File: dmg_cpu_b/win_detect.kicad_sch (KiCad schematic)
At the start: 127 parts

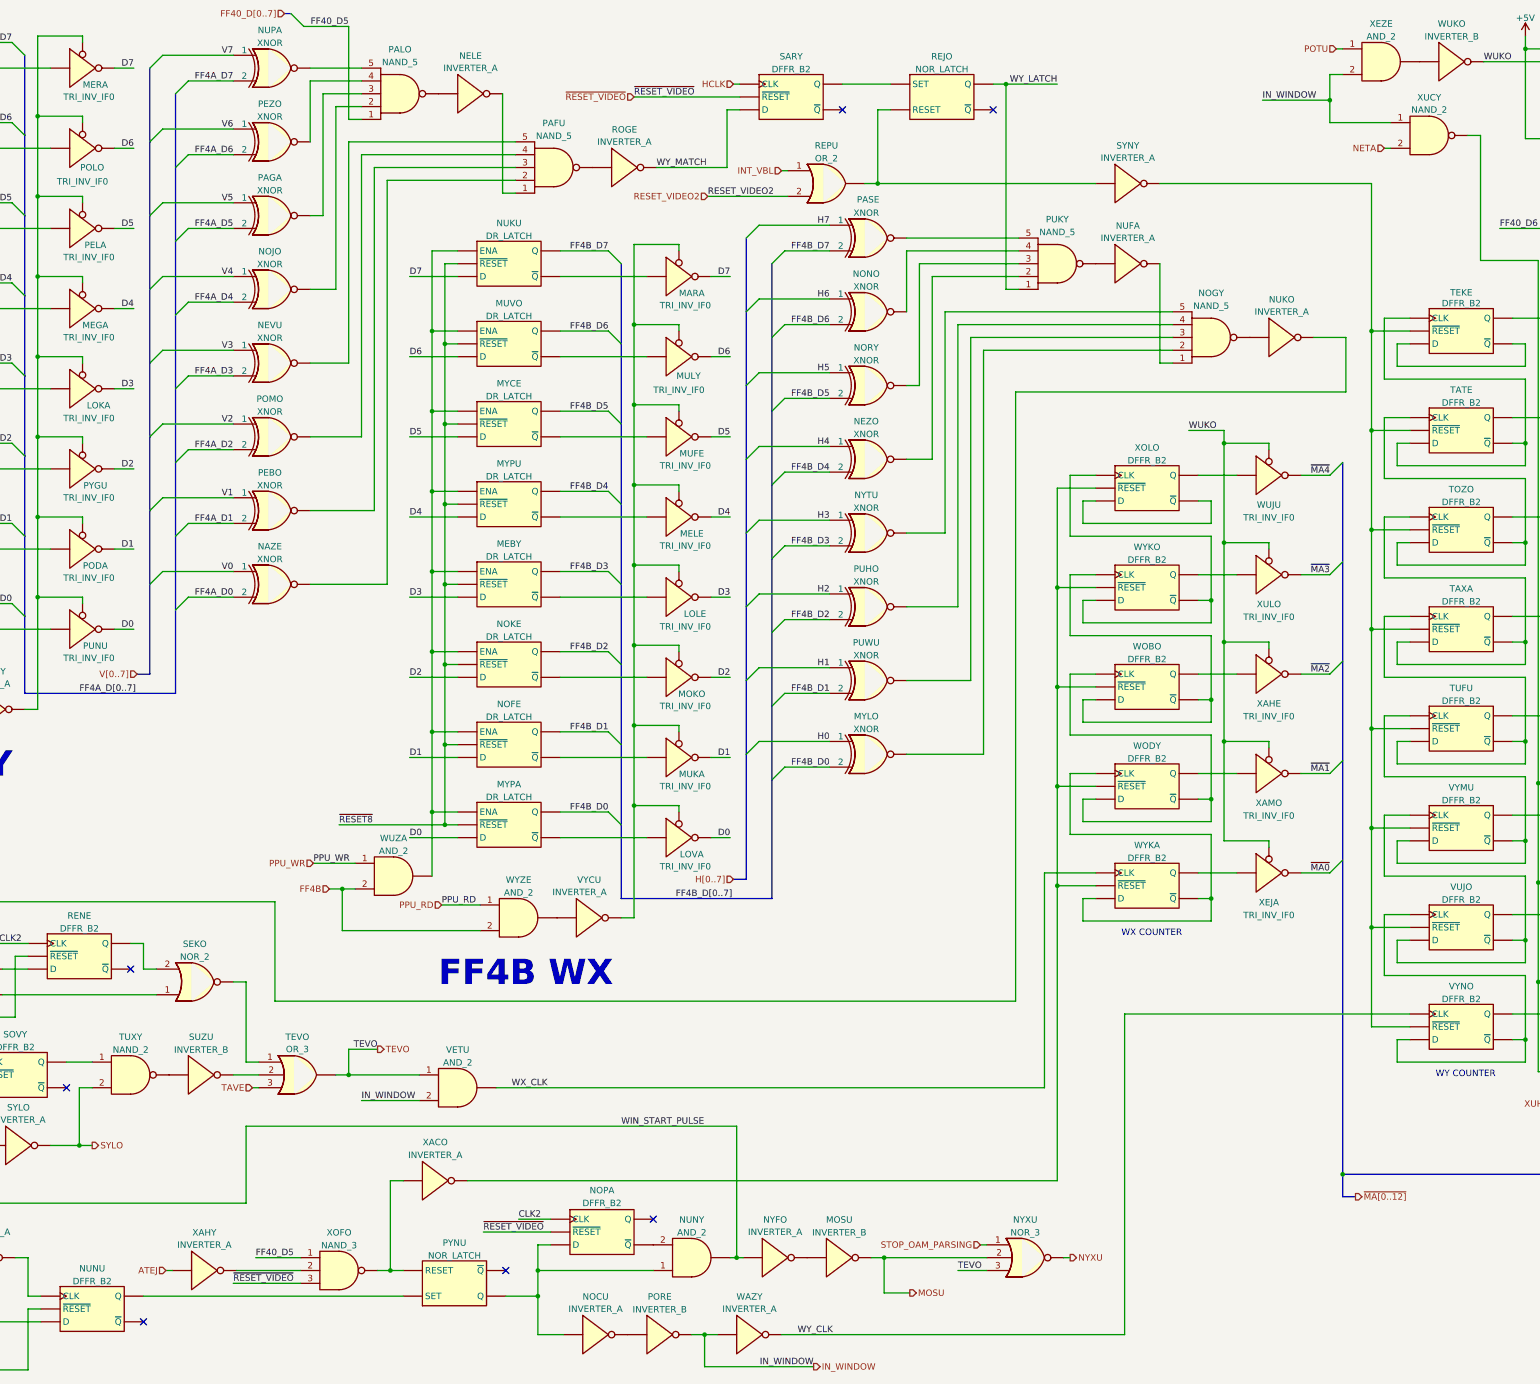
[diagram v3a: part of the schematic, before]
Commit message: More OAM sheets added.
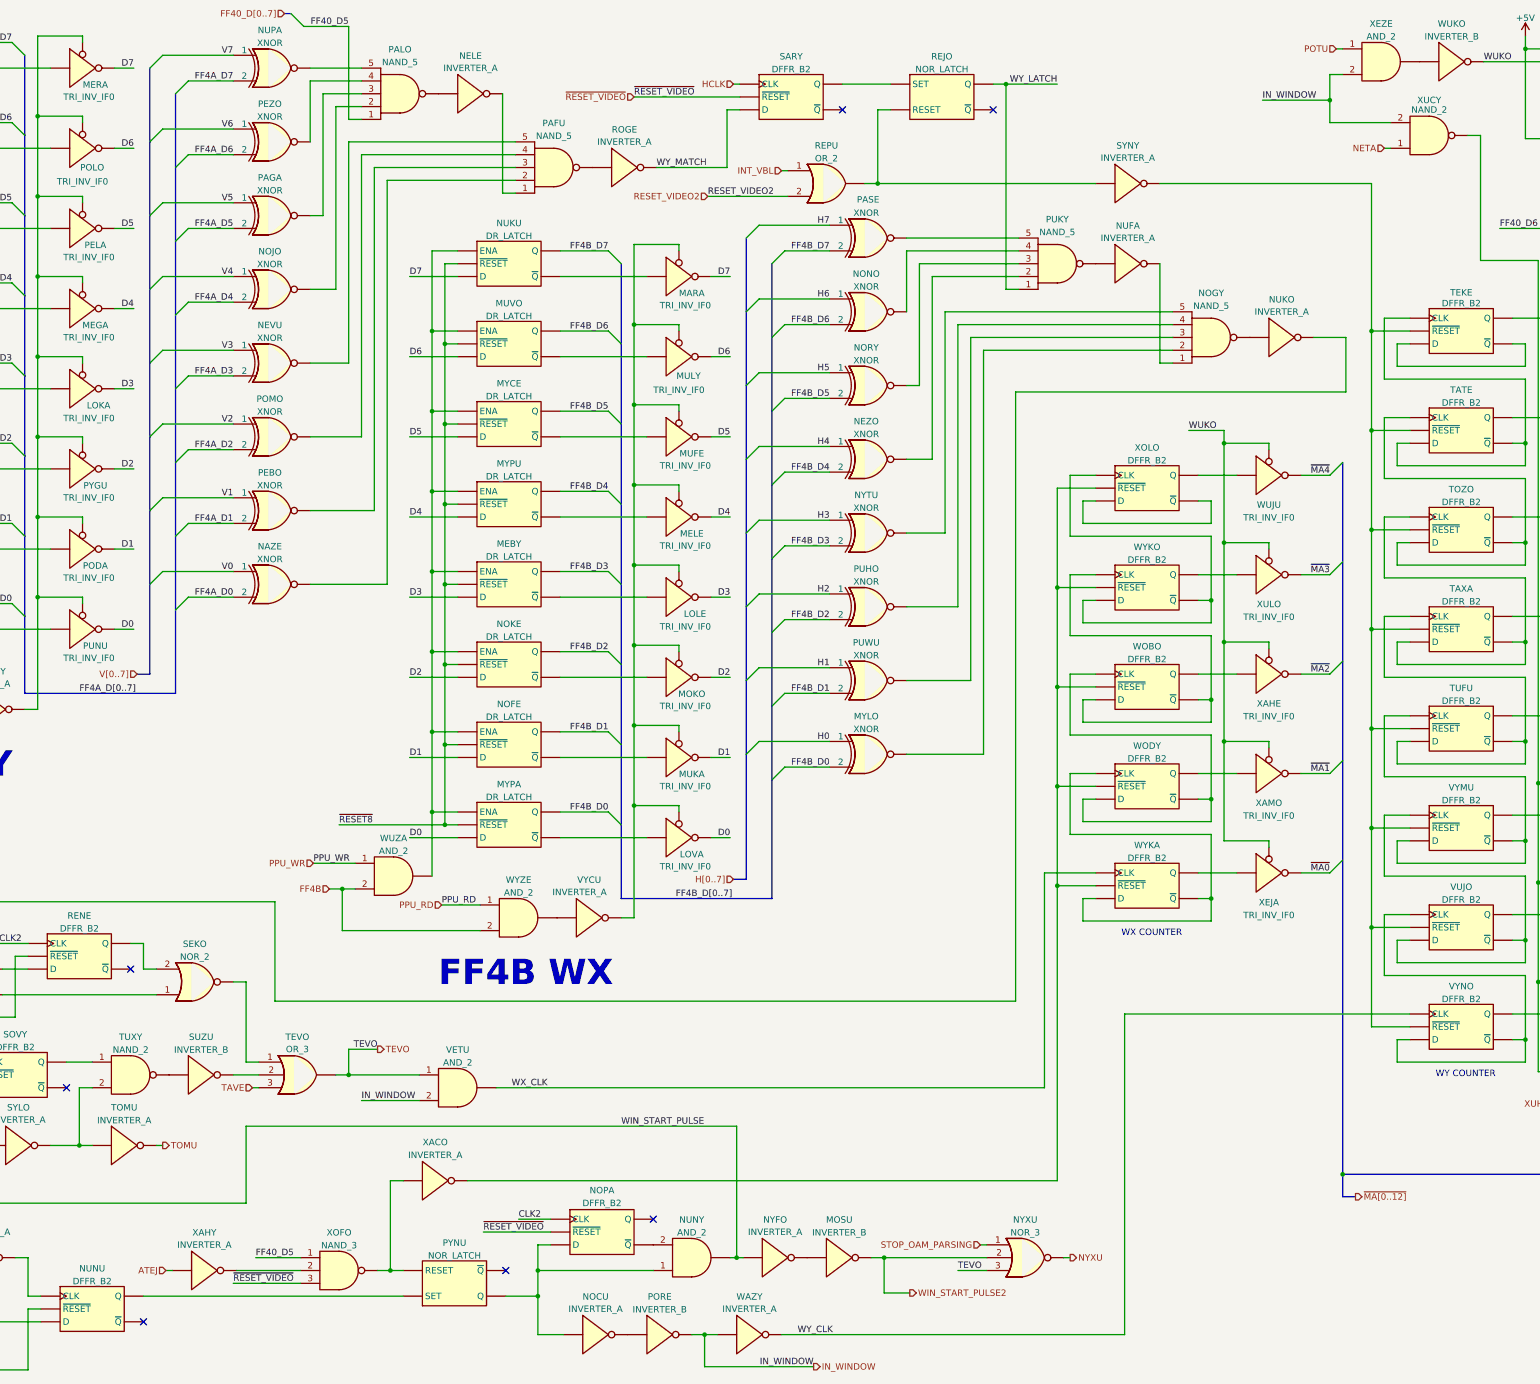
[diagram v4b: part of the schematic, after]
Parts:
- added TOMU: INVERTER_A, symbol DMG_CPU_Cells:INVERTER_A
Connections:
- net IN_WINDOW: now also XUCY.2; no longer XUCY.1
- net NETA: now also XUCY.1; no longer XUCY.2
- net MOSU renamed WIN_START_PULSE2
- net SYLO: no longer names the net of SYLO.2, TUXY.2
- net SYLO: now also TOMU.1
- new net TOMU: TOMU.2
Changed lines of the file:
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@@
     (stroke (width 0) (type default) (color 0 0 0 0))
   )
-  (wire (pts (xy 90.17 238.76) (xy 92.71 238.76))
-    (stroke (width 0) (type default) (color 0 0 0 0))
-  )
   (wire (pts (xy 124.46 227.33) (xy 125.73 227.33))
     (stroke (width 0) (type default) (color 0 0 0 0))
@@
     (stroke (width 0) (type default) (color 0 0 0 0))
   )
+  (wire (pts (xy 90.17 238.76) (xy 92.71 238.76))
+    (stroke (width 0) (type default) (color 0 0 0 0))
+  )
   (wire (pts (xy 254 88.265) (xy 256.54 88.265))
     (stroke (width 0) (type default) (color 0 0 0 0))
@@
     (stroke (width 0) (type default) (color 0 0 0 0))
   )
+  (wire (pts (xy 105.41 238.76) (xy 106.68 238.76))
+    (stroke (width 0) (type default) (color 0 0 0 0))
+  )
   (wire (pts (xy 97.155 73.025) (xy 100.965 73.025))
     (stroke (width 0) (type default) (color 0 0 0 0))
@@
     (effects (font (size 1.27 1.27)) (justify right))
   )
-  (hierarchical_label "SYLO" (shape output) (at 92.71 238.76 0)
-    (effects (font (size 1.27 1.27)) (justify left))
-  )
   (hierarchical_label "ATEJ" (shape input) (at 107.315 263.525 180)
     (effects (font (size 1.27 1.27)) (justify right))
   )
-  (hierarchical_label "MOSU" (shape output) (at 254.635 267.97 0)
+  (hierarchical_label "WIN_START_PULSE2" (shape output) (at 254.635 267.97 0)
     (effects (font (size 1.27 1.27)) (justify left))
   )
@@
     (effects (font (size 1.27 1.27)) (justify right))
   )
+  (hierarchical_label "TOMU" (shape output) (at 106.68 238.76 0)
+    (effects (font (size 1.27 1.27)) (justify left))
+  )
   (hierarchical_label "ROZE" (shape input) (at 27.94 206.375 180)
     (effects (font (size 1.27 1.27)) (justify right))
@@
     (pin "1")
   )
-  (symbol (lib_id "DMG_CPU_Cells:NAND_2") (at 357.505 38.735 0) (unit 1)
+  (symbol (lib_id "DMG_CPU_Cells:NAND_2") (at 357.505 38.735 0) (mirror x) (unit 1)
     (in_bom yes) (on_board yes)
-    (property "Reference" "XUCY" (id 0) (at 357.505 31.2252 0))
+    (property "Reference" "XUCY" (id 0) (at 357.505 31.75 0))
     (property "Value" "NAND_2" (id 1) (at 357.505 33.655 0))
     (property "Footprint" "" (id 2) (at 357.505 38.735 0)
       (effects (font (size 1.27 1.27)) hide)
     )
-    (property "Datasheet" "http://iceboy.a-singer.de/doc/dmg_cells.html#nand2" (id 3) (at 357.505 46.355 0)
+    (property "Datasheet" "http://iceboy.a-singer.de/doc/dmg_cells.html#nand2" (id 3) (at 357.505 31.115 0)
       (effects (font (size 1.27 1.27)) hide)
     )
@@
       (effects (font (size 1.27 1.27)) hide)
     )
+    (pin "1")
+    (pin "2")
+  )
+  (symbol (lib_id "DMG_CPU_Cells:INVERTER_A") (at 99.06 238.76 0) (unit 1)
+    (in_bom yes) (on_board yes) (fields_autoplaced)
+    (property "Reference" "TOMU" (id 0) (at 99.06 231.2502 0))
+    (property "Value" "INVERTER_A" (id 1) (at 99.06 233.7871 0))
+    (property "Footprint" "" (id 2) (at 96.52 238.76 0)
+      (effects (font (size 1.27 1.27)) hide)
+    )
+    (property "Datasheet" "http://iceboy.a-singer.de/doc/dmg_cells.html#inv_a" (id 3) (at 100.33 246.38 0)
+      (effects (font (size 1.27 1.27)) hide)
+    )

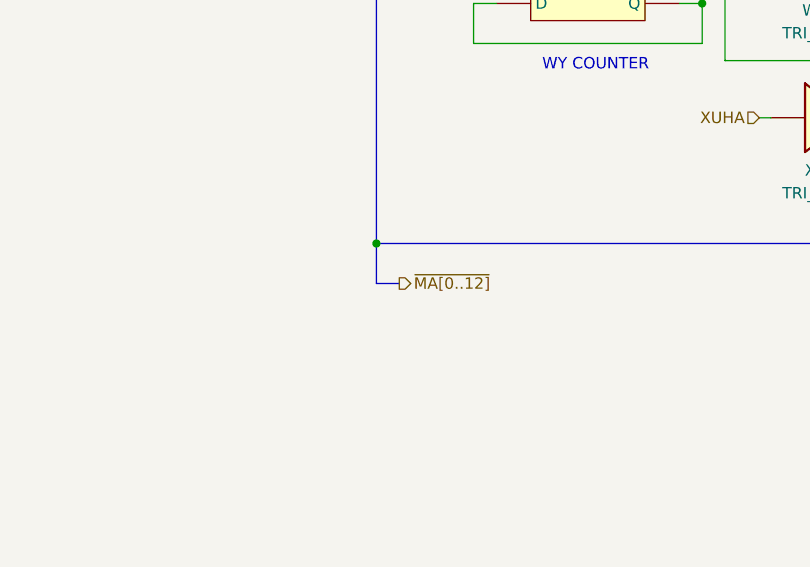
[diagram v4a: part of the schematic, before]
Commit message: bg and sp px shifters added.
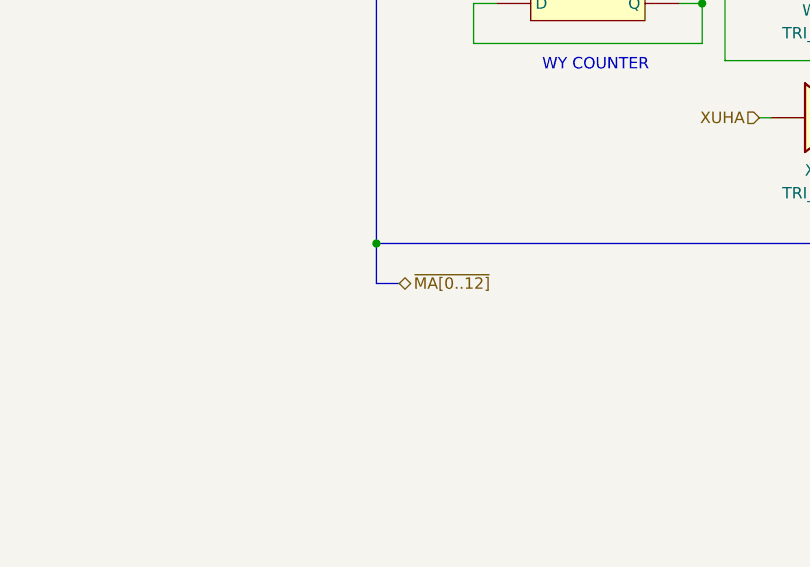
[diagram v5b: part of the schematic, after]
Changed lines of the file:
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@@
     (effects (font (size 1.27 1.27)) (justify right))
   )
-  (hierarchical_label "~{MA[0..12]}" (shape output) (at 342.9 248.92 0)
+  (hierarchical_label "~{MA[0..12]}" (shape tri_state) (at 342.9 248.92 0)
     (effects (font (size 1.27 1.27)) (justify left))
   )

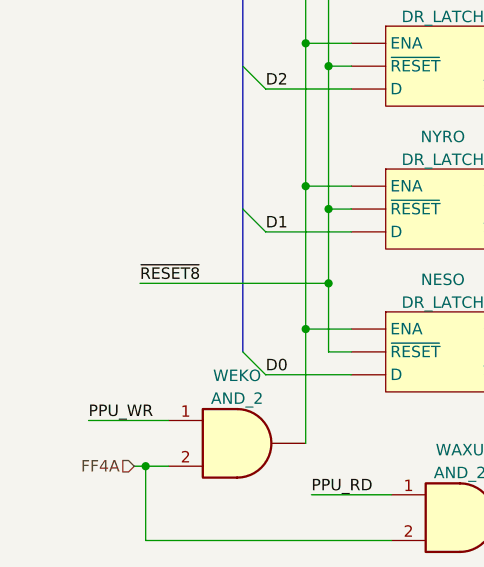
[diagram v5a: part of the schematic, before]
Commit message: All sheets captured. Serious tidying is required in PPU section.
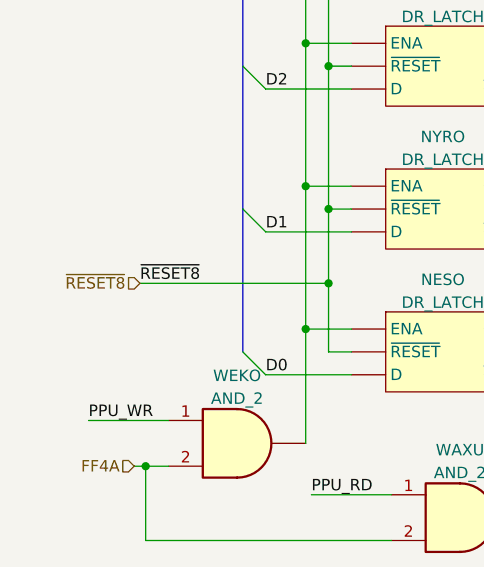
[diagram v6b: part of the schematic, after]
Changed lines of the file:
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@@
   (title_block
     (title "DMG CPU B")
-    (date "2022-05-02")
+    (date "2022-05-19")
     (rev "0")
     (company "CC-BY-SA-4.0 Régis Galland & Michael Singer -- Derived work from Furrtek")
@@
     (effects (font (size 1.27 1.27)) (justify right))
   )
+  (hierarchical_label "~{RESET8}" (shape input) (at 23.495 126.365 180)
+    (effects (font (size 1.27 1.27)) (justify right))
+  )

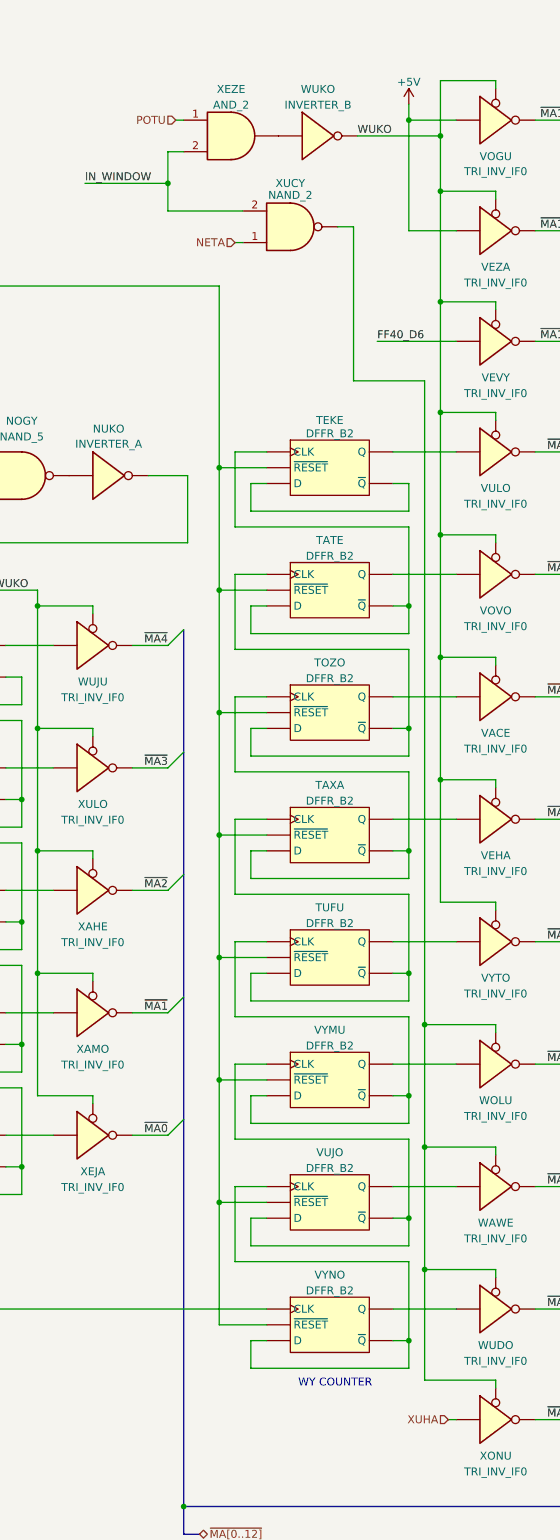
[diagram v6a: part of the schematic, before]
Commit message: New sheet created to free up space on LCD and SCX/SCY sheets and joined common signals.
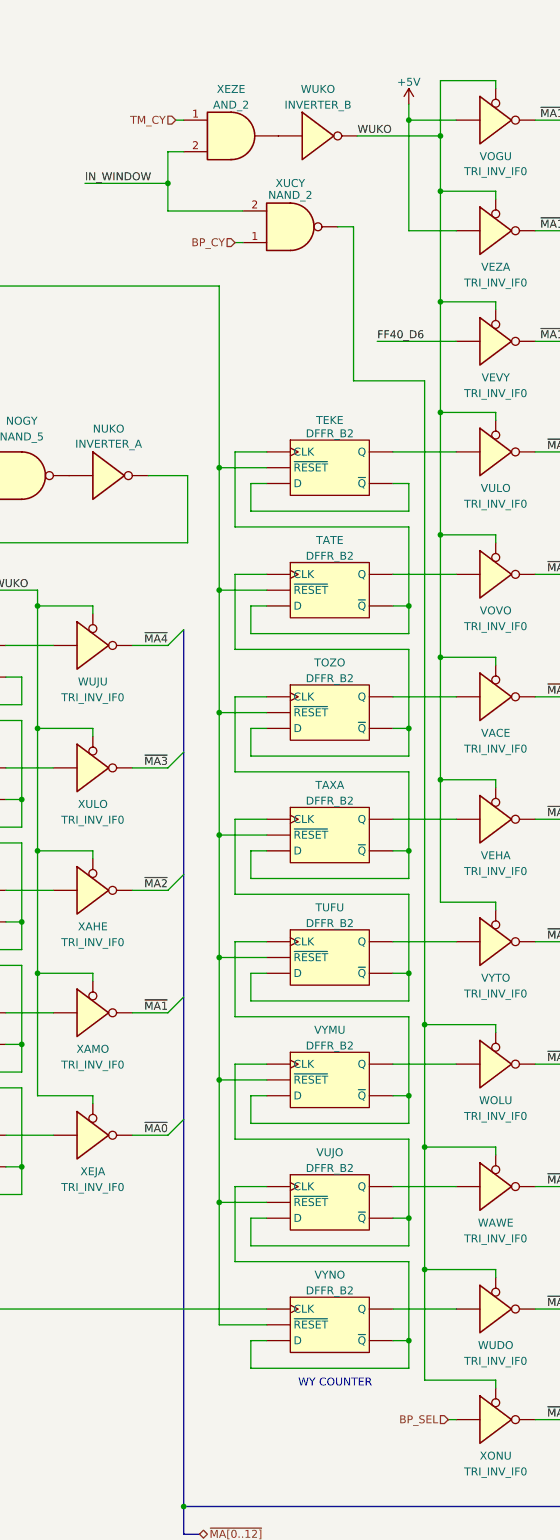
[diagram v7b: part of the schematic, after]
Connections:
- net NETA renamed BP_CY
- net POTU renamed TM_CY
- net XUHA renamed BP_SEL
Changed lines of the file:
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@@
     (effects (font (size 1.27 1.27)) (justify right))
   )
-  (hierarchical_label "NETA" (shape input) (at 348.615 41.275 180)
+  (hierarchical_label "BP_CY" (shape input) (at 348.615 41.275 180)
     (effects (font (size 1.27 1.27)) (justify right))
   )
@@
     (effects (font (size 1.27 1.27)) (justify right))
   )
-  (hierarchical_label "XUHA" (shape input) (at 382.905 230.505 180)
+  (hierarchical_label "BP_SEL" (shape input) (at 382.905 230.505 180)
     (effects (font (size 1.27 1.27)) (justify right))
   )
@@
     (effects (font (size 1.27 1.27)) (justify right))
   )
-  (hierarchical_label "POTU" (shape input) (at 339.09 21.59 180)
+  (hierarchical_label "TM_CY" (shape input) (at 339.09 21.59 180)
     (effects (font (size 1.27 1.27)) (justify right))
   )

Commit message: PPU hierarchical page progress. Elements moved out of window sheet to be includes in BG and WIN cycles sheet
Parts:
- removed MEHE, NOCU, NYFO, ROCO, SYLO, TOMU, XACO, XAHY: INVERTER_A, symbol DMG_CPU_Cells:INVERTER_A
- removed MOSU, PORE, SUZU: INVERTER_B, symbol DMG_CPU_Cells:INVERTER_B
- removed NOPA, NUNU, PYCO, RENE, RYFA, SOVY: DFFR_B2, symbol DMG_CPU_Cells:DFFR_B2
- removed NUNY, VETU: AND_2, symbol DMG_CPU_Cells:AND_2
- removed NYXU, RYDY: NOR_3, symbol DMG_CPU_Cells:NOR_3
- removed PANY, PUKU, SEKO: NOR_2, symbol DMG_CPU_Cells:NOR_2
- removed PYNU: NOR_LATCH, symbol DMG_CPU_Cells:NOR_LATCH
- removed TEVO: OR_3, symbol DMG_CPU_Cells:OR_3
- removed TUXY: NAND_2, symbol DMG_CPU_Cells:NAND_2
- removed XOFO: NAND_3, symbol DMG_CPU_Cells:NAND_3
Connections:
- net ~{WX_RST}: now reaches WOBO.2 (~{RESET}), WOBO.4 (~{RESET}), WODY.2 (~{RESET}), WODY.4 (~{RESET}), WYKA.2 (~{RESET}), WYKA.4 (~{RESET}), WYKO.2 (~{RESET}), WYKO.4 (~{RESET}), XOLO.2 (~{RESET}), XOLO.4 (~{RESET})
- no-connect marks 8 -> 2
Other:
- moved on the sheet: WAZY, WOBO, WODY, WUJU, WYKA, WYKO, XAHE, XAMO, XEJA, XOLO, XULO
